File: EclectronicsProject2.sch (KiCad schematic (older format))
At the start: 79 parts, among them J7 Barrel_Jack, U11 TPS62290DRVR, U8 TPS62290DRVR

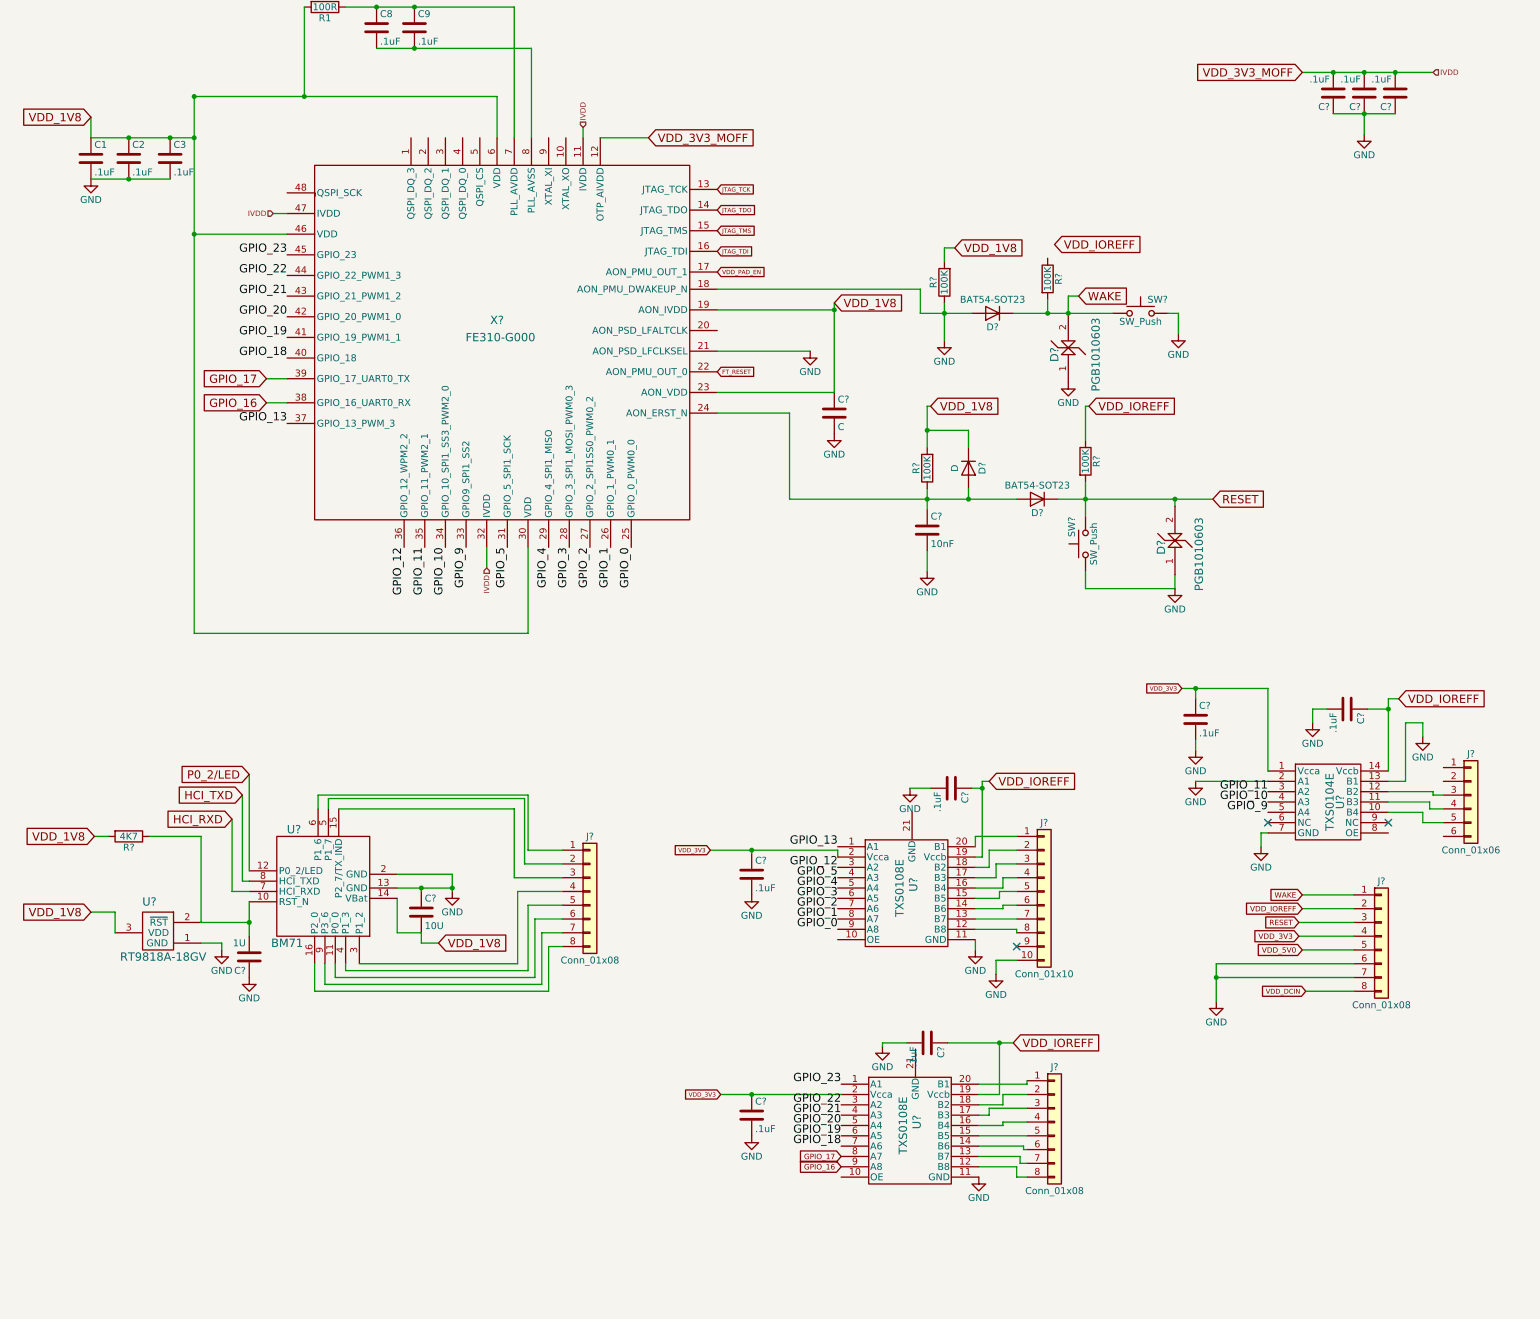
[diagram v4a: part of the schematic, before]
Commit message: added flash memory
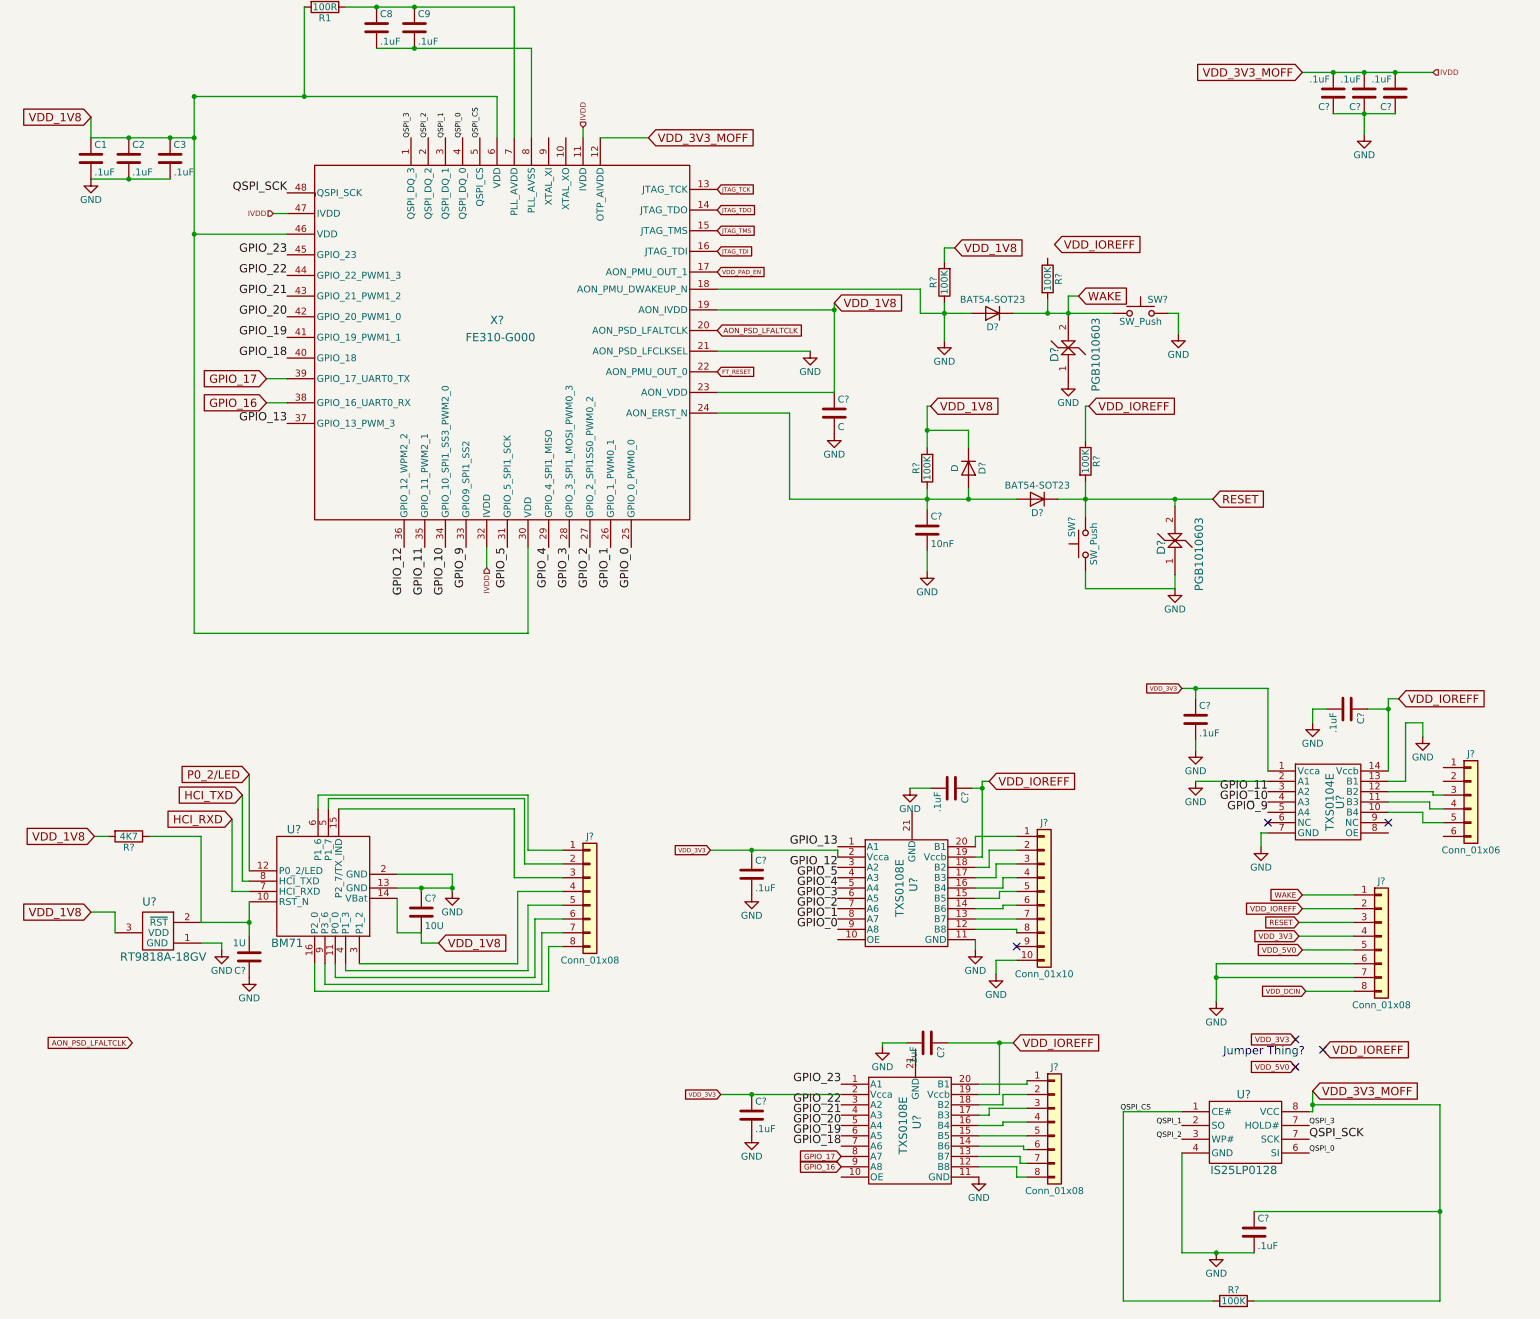
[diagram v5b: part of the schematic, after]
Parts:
- added C?: .1uF, symbol C
- added R?: 100K, symbol R
- added U?: IS25LP0128, symbol IS25LP0128
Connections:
- net GND: now also C?.2, U?.4 (GND)
- net VDD_3V3_MOFF: now also C?.1, R?.2, U?.8 (VCC)
- net QSPI_3: now reaches X?.1 (QSPI_DQ_3)
- net QSPI_3: now also U?.7 (SCK)
- net QSPI_2: now reaches X?.2 (QSPI_DQ_2)
- net QSPI_2: now also U?.3 (WP#)
- net AON_PSD_LFALTCLK: now reaches X?.20 (AON_PSD_LFALTCLK)
- net QSPI_1: now reaches X?.3 (QSPI_DQ_1)
- net QSPI_1: now also U?.2 (SO)
- net QSPI_0: now reaches X?.4 (QSPI_DQ_0)
- net QSPI_0: now also U?.6 (SI)
- net QSPI_SCK: now reaches X?.48 (QSPI_SCK)
- net QSPI_SCK: now also U?.7 (SCK)
- net QSPI_CS: now reaches X?.5 (QSPI_CS)
- net QSPI_CS: now also R?.1, U?.1 (CE#)
- no-connect marks 4 -> 7
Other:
- note added: "Jumper Thing?\n"
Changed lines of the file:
@@
 	10175 7600 9175 7600
 Connection ~ 9175 7600
+Text GLabel 9750 8250 0    39   Input ~ 0
+VDD_5V0
+Text GLabel 9750 8050 0    39   Input ~ 0
+VDD_3V3
+Text GLabel 9950 8125 2    60   Input ~ 0
+VDD_IOREFF
+NoConn ~ 9750 8050
+NoConn ~ 9950 8125
+NoConn ~ 9750 8250
+Text Notes 9225 8175 0    60   ~ 0
+Jumper Thing?\n
+$Comp
+L IS25LP0128 U?
+U 1 1 59D012A5
+P 9375 8725
+F 0 "U?" H 9375 9000 60  0000 C CNN
+F 1 "IS25LP0128" H 9375 8450 60  0000 C CNN
+F 2 "" H 9375 8725 60  0001 C CNN
+F 3 "" H 9375 8725 60  0001 C CNN
+	1    9375 8725
+	1    0    0    -1
+$EndComp
+Text GLabel 9875 8425 2    60   Input ~ 0
+VDD_3V3_MOFF
+Wire Wire Line
+	9875 8425 9875 8575
+Wire Wire Line
+	9875 8575 9850 8575
+$Comp
+L GND #PWR?
+U 1 1 59D01D65
+P 9175 9600
+F 0 "#PWR?" H 9175 9350 50  0001 C CNN
+F 1 "GND" H 9175 9450 50  0000 C CNN
+F 2 "" H 9175 9600 50  0001 C CNN
+F 3 "" H 9175 9600 50  0001 C CNN
+	1    9175 9600
+	1    0    0    -1
+$EndComp
+$Comp
+L C C?
+U 1 1 59D01EB0
+P 9450 9450
+F 0 "C?" H 9475 9550 50  0000 L CNN
+F 1 ".1uF" H 9475 9350 50  0000 L CNN
+F 2 "" H 9488 9300 50  0001 C CNN
+F 3 "" H 9450 9450 50  0001 C CNN
+	1    9450 9450
+	1    0    0    -1
+$EndComp
+Wire Wire Line
+	9875 8525 10800 8525
+Wire Wire Line
+	10800 8525 10800 9950
+Wire Wire Line
+	10800 9300 9450 9300
+Connection ~ 9875 8525
+Wire Wire Line
+	8925 8875 8925 9600
+Wire Wire Line
+	8925 9600 9450 9600
+Connection ~ 9175 9600
+$Comp
+L R R?
+U 1 1 59D02BD3
+P 9300 9950
+F 0 "R?" V 9380 9950 50  0000 C CNN
+F 1 "100K" V 9300 9950 50  0000 C CNN
+F 2 "" V 9230 9950 50  0001 C CNN
+F 3 "" H 9300 9950 50  0001 C CNN
+	1    9300 9950
+	0    -1   -1   0
+$EndComp
+Wire Wire Line
+	8925 8575 8500 8575
+Wire Wire Line
+	8500 8575 8500 9950
+Wire Wire Line
+	8500 9950 9150 9950
+Wire Wire Line
+	10800 9950 9450 9950
+Connection ~ 10800 9300
+Text Label 9850 8775 0    60   ~ 0
+QSPI_SCK
+Text Label 2425 1900 2    60   ~ 0
+QSPI_SCK
+Text Label 3575 1500 1    39   ~ 0
+QSPI_1
+Text Label 3450 1500 1    39   ~ 0
+QSPI_2
+Text Label 3325 1500 1    39   ~ 0
+QSPI_3
+Text Label 3700 1500 1    39   ~ 0
+QSPI_0
+Text Label 9850 8875 0    39   ~ 0
+QSPI_0
+Text Label 8925 8675 2    39   ~ 0
+QSPI_1
+Text Label 8925 8775 2    39   ~ 0
+QSPI_2
+Text Label 9850 8675 0    39   ~ 0
+QSPI_3
+Text Label 8700 8575 2    39   ~ 0
+QSPI_CS
+Text Label 3825 1500 1    39   ~ 0
+QSPI_CS
+Text GLabel 5550 2900 2    39   Input ~ 0
+AON_PSD_LFALTCLK
+Text GLabel 1300 8075 0    39   Input ~ 0
+AON_PSD_LFALTCLK
 $EndSCHEMATC

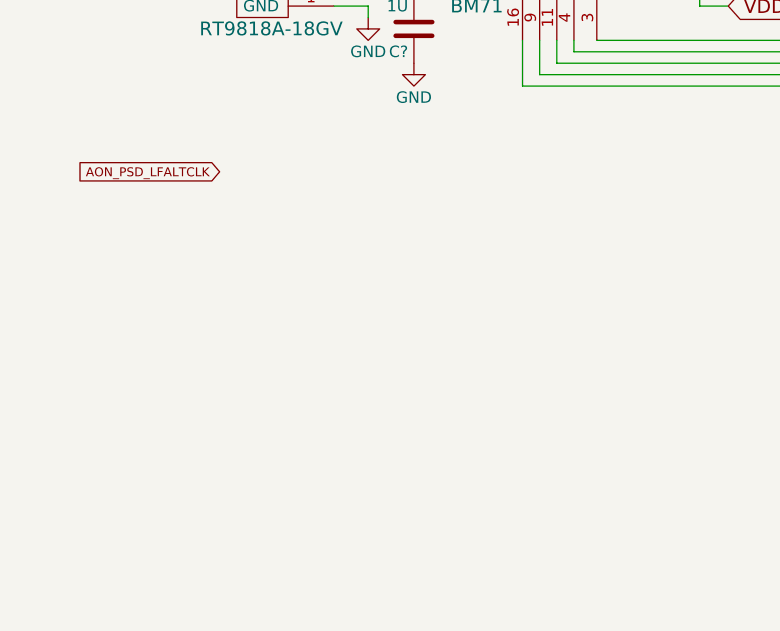
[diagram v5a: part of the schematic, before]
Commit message: added 32MHz clock
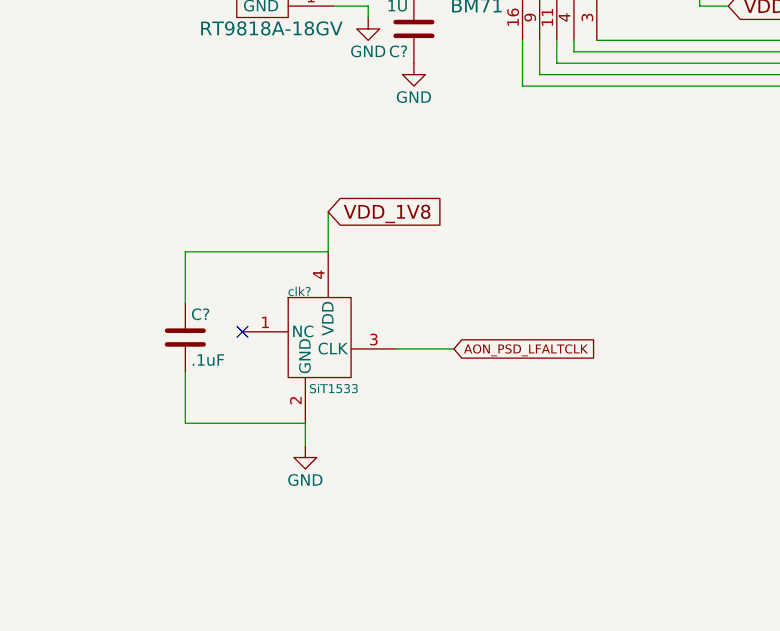
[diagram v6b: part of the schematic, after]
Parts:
- added C?: .1uF, symbol C
- added clk?: SiT1533, symbol SiT1533
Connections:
- net AON_PSD_LFALTCLK: now also clk?.3 (CLK)
- net GND: now also C?.2, clk?.2 (GND)
- net TP1: now also C?.1, clk?.4 (VDD)
- no-connect marks 7 -> 8
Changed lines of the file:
@@
 Text GLabel 5550 2900 2    39   Input ~ 0
 AON_PSD_LFALTCLK
-Text GLabel 1300 8075 0    39   Input ~ 0
+Text GLabel 2325 8850 2    39   Input ~ 0
 AON_PSD_LFALTCLK
+$Comp
+L SiT1533 clk?
+U 1 1 59D08D13
+P 1725 8800
+F 0 "clk?" H 1650 9000 39  0000 C CNN
+F 1 "SiT1533" H 1800 8575 39  0000 C CNN
+F 2 "" H 1725 8800 39  0001 C CNN
+F 3 "" H 1725 8800 39  0001 C CNN
+	1    1725 8800
+	1    0    0    -1
+$EndComp
+$Comp
+L C C?
+U 1 1 59D090D3
+P 1150 8800
+F 0 "C?" H 1175 8900 50  0000 L CNN
+F 1 ".1uF" H 1175 8700 50  0000 L CNN
+F 2 "" H 1188 8650 50  0001 C CNN
+F 3 "" H 1150 8800 50  0001 C CNN
+	1    1150 8800
+	1    0    0    -1
+$EndComp
+NoConn ~ 1400 8775
+Wire Wire Line
+	1775 8425 1150 8425
+Wire Wire Line
+	1150 8425 1150 8650
+$Comp
+L GND #PWR?
+U 1 1 59D09830
+P 1675 9275
+F 0 "#PWR?" H 1675 9025 50  0001 C CNN
+F 1 "GND" H 1675 9125 50  0000 C CNN
+F 2 "" H 1675 9275 50  0001 C CNN
+F 3 "" H 1675 9275 50  0001 C CNN
+	1    1675 9275
+	1    0    0    -1
+$EndComp
+Wire Wire Line
+	1150 8950 1150 9175
+Wire Wire Line
+	1150 9175 1675 9175
+Wire Wire Line
+	1675 9175 1675 9275
+Text GLabel 1775 8250 2    60   Input ~ 0
+VDD_1V8
+Wire Wire Line
+	1775 8250 1775 8425
+Wire Wire Line
+	2325 8850 2075 8850
 $EndSCHEMATC
